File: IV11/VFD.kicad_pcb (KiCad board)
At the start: 2 copper layers, 225 x 80 mm, 71 parts, among them J1 USB_B, SW1 switch, SW2 switch, SW3 switch, SW4 switch, U1 74HC595, U10 UDN2981, U11 UDN2981, U12 UDN2981, U13 WeMos_mini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

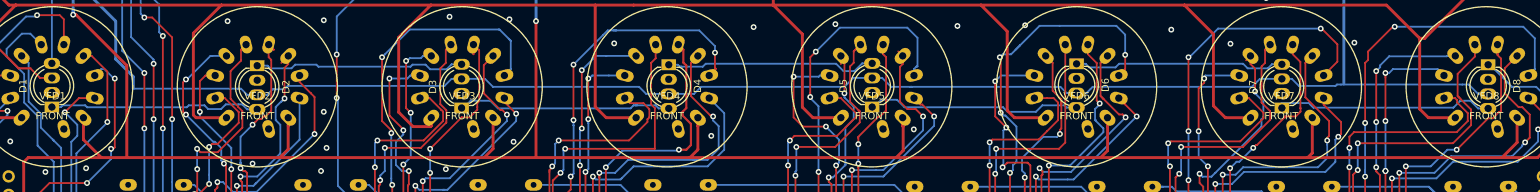
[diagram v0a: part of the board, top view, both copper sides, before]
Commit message: Make LED footprint pads slightly narrower (1.3mm) for easier solderingx
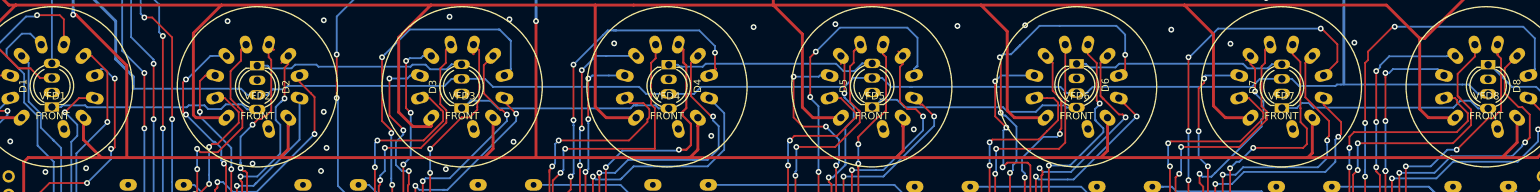
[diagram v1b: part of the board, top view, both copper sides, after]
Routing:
- net Net-(U16-Pad11): track 48.4 -> 52.2 mm
- net Net-(U16-Pad17): track 37.3 -> 36.6 mm

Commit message: s/chinesemodules/genericmodules
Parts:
- U18: footprint ChineseModules:BuckModule -> GenericModules:MP2307BuckConverterModule
- U19: footprint ChineseModules:MT3608BoostModule -> GenericModules:MT3608BoostConverterModule
- U20: footprint ChineseModules:DS3121RTCModule -> GenericModules:DS3121RTCModule
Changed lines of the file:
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@@
-(kicad_pcb (version 20171130) (host pcbnew 5.0.0-fee4fd1~66~ubuntu18.04.1)
+(kicad_pcb (version 20171130) (host pcbnew 5.0.0-fee4fd1~65~ubuntu17.10.1)
   (general
     (thickness 1.6)
@@
     )
   )
-  (module ChineseModules:BuckModule (layer B.Cu)
-    (at 113.538 19.812 180)
-    (fp_text reference U18 (at 0 2.286 180) (layer B.SilkS)
-      (effects (font (size 1 1) (thickness 0.15)) (justify mirror))
-    )
-    (fp_text value MiniBuckBoard (at 0 0.5 180) (layer B.Fab)
-      (effects (font (size 1 1) (thickness 0.15)) (justify mirror))
-    )
-    (fp_text user GND (at 5 -5 180) (layer B.SilkS)
-      (effects (font (size 1 1) (thickness 0.15)) (justify mirror))
-    )
-    (fp_text user GND (at -5 -5 180) (layer B.SilkS)
-      (effects (font (size 1 1) (thickness 0.15)) (justify mirror))
-    )
-    (fp_text user Vout (at -5 5 180) (layer B.SilkS)
-      (effects (font (size 1 1) (thickness 0.15)) (justify mirror))
-    )
-    (fp_text user Vin (at 5 5 180) (layer B.SilkS)
-      (effects (font (size 1 1) (thickness 0.15)) (justify mirror))
-    )
-    (fp_line (start -9.25 6) (end -9.25 -6) (layer B.SilkS) (width 0.15))
-    (fp_line (start -9.25 -6) (end 9.25 -6) (layer B.SilkS) (width 0.15))
-    (fp_line (start 9.25 6) (end 9.25 -6) (layer B.SilkS) (width 0.15))
-    (fp_line (start -9.25 6) (end 9.25 6) (layer B.SilkS) (width 0.15))
-    (pad 4 thru_hole oval (at 8 5 180) (size 2.4 1.6) (drill 1) (layers *.Cu *.Mask)
-      (net 147 +5V))
-    (pad 3 thru_hole oval (at 8 -5 180) (size 2.4 1.6) (drill 1) (layers *.Cu *.Mask)
-      (net 1 GND))
-    (pad 2 thru_hole oval (at -8 -5 180) (size 2.4 1.6) (drill 1) (layers *.Cu *.Mask)
-      (net 1 GND))
-    (pad 1 thru_hole oval (at -8 5 180) (size 2.4 1.6) (drill 1) (layers *.Cu *.Mask)
-      (net 12 +1V5))
-  )
   (module "" (layer F.Cu)
     (at 102.997 2.54)
@@
     )
   )
-  (module ChineseModules:MT3608BoostModule (layer B.Cu)
+  (module GenericModules:MP2307BuckConverterModule (layer B.Cu)
+    (at 113.538 19.812 180)
+    (fp_text reference U18 (at 0 -1 180) (layer B.SilkS)
+      (effects (font (size 1 1) (thickness 0.15)) (justify mirror))
+    )
+    (fp_text value MiniBuckBoard (at 0 0.5 180) (layer B.Fab)
+      (effects (font (size 1 1) (thickness 0.15)) (justify mirror))
+    )
+    (fp_line (start -9.25 6) (end 9.25 6) (layer B.SilkS) (width 0.15))
+    (fp_line (start 9.25 6) (end 9.25 -6) (layer B.SilkS) (width 0.15))
+    (fp_line (start -9.25 -6) (end 9.25 -6) (layer B.SilkS) (width 0.15))
+    (fp_line (start -9.25 6) (end -9.25 -6) (layer B.SilkS) (width 0.15))
+    (fp_text user Vin (at 5 5 180) (layer B.SilkS)
+      (effects (font (size 1 1) (thickness 0.15)) (justify mirror))
+    )
+    (fp_text user Vout (at -5 5 180) (layer B.SilkS)
+      (effects (font (size 1 1) (thickness 0.15)) (justify mirror))
+    )
+    (fp_text user GND (at -5 -5 180) (layer B.SilkS)
+      (effects (font (size 1 1) (thickness 0.15)) (justify mirror))
+    )
+    (fp_text user GND (at 5 -5 180) (layer B.SilkS)
+      (effects (font (size 1 1) (thickness 0.15)) (justify mirror))
+    )
+    (pad 1 thru_hole oval (at -8 5 180) (size 2.4 1.6) (drill 1) (layers *.Cu *.Mask)
+      (net 12 +1V5))
+    (pad 2 thru_hole oval (at -8 -5 180) (size 2.4 1.6) (drill 1) (layers *.Cu *.Mask)
+      (net 1 GND))
+    (pad 3 thru_hole oval (at 8 -5 180) (size 2.4 1.6) (drill 1) (layers *.Cu *.Mask)
+      (net 1 GND))
+    (pad 4 thru_hole oval (at 8 5 180) (size 2.4 1.6) (drill 1) (layers *.Cu *.Mask)
+      (net 147 +5V))
+  )
+  (module GenericModules:MT3608BoostConverterModule (layer B.Cu)
     (at 94.361 2.159 180)
     (fp_text reference U19 (at 15 -9 180) (layer B.SilkS)
@@
       (net 147 +5V))
   )
-  (module ChineseModules:DS3121RTCModule (layer B.Cu)
+  (module GenericModules:DS3121RTCModule (layer B.Cu)
     (at 143.002 9.779 180)
     (fp_text reference U20 (at 0 -2 180) (layer B.SilkS)
@@
       (effects (font (size 1 1) (thickness 0.15)) (justify mirror))
     )
-    (fp_text user UPPERMOST (at 0 -8 180) (layer B.SilkS)
+    (fp_line (start -19 9) (end 18.25 9) (layer B.SilkS) (width 0.15))
+    (fp_line (start -19 9) (end -19 -13.25) (layer B.SilkS) (width 0.15))
+    (fp_line (start -19 -13.25) (end 18.25 -13.25) (layer B.SilkS) (width 0.15))
+    (fp_line (start 18.25 9) (end 18.25 -13.25) (layer B.SilkS) (width 0.15))
+    (fp_text user "COIN CELL" (at 0 -6 180) (layer B.SilkS)
       (effects (font (size 1 1) (thickness 0.15)) (justify mirror))
     )
-    (fp_text user "COIN CELL" (at 0 -6 180) (layer B.SilkS)
+    (fp_text user UPPERMOST (at 0 -8 180) (layer B.SilkS)
       (effects (font (size 1 1) (thickness 0.15)) (justify mirror))
     )
-    (fp_line (start 18.25 9) (end 18.25 -13.25) (layer B.SilkS) (width 0.15))
-    (fp_line (start -19 -13.25) (end 18.25 -13.25) (layer B.SilkS) (width 0.15))
-    (fp_line (start -19 9) (end -19 -13.25) (layer B.SilkS) (width 0.15))
-    (fp_line (start -19 9) (end 18.25 9) (layer B.SilkS) (width 0.15))
-    (pad 6 thru_hole oval (at -17.25 -8.475 180) (size 2.4 1.6) (drill 1) (layers *.Cu *.Mask)
-      (net 152 "Net-(U20-Pad6)"))
-    (pad 7 thru_hole oval (at 16.5 -5.935 180) (size 2.4 1.6) (drill 1) (layers *.Cu *.Mask)
-      (net 155 "Net-(U20-Pad7)"))
-    (pad 8 thru_hole oval (at 16.5 -3.395 180) (size 2.4 1.6) (drill 1) (layers *.Cu *.Mask)
-      (net 154 "Net-(U20-Pad8)"))
-    (pad 9 thru_hole oval (at 16.5 -0.855 180) (size 2.4 1.6) (drill 1) (layers *.Cu *.Mask)
-      (net 153 "Net-(U20-Pad9)"))
-    (pad 10 thru_hole oval (at 16.5 1.685 180) (size 2.4 1.6) (drill 1) (layers *.Cu *.Mask)
-      (net 1 GND))
-    (pad 1 thru_hole oval (at -17.25 4.225 180) (size 2.4 1.6) (drill 1) (layers *.Cu *.Mask)
-      (net 1 GND))
-    (pad 2 thru_hole oval (at -17.25 1.685 180) (size 2.4 1.6) (drill 1) (layers *.Cu *.Mask)
-      (net 150 +3V3))
-    (pad 5 thru_hole oval (at -17.25 -5.935 180) (size 2.4 1.6) (drill 1) (layers *.Cu *.Mask)
-      (net 151 "Net-(U20-Pad5)"))
-    (pad 3 thru_hole oval (at -17.25 -0.855 180) (size 2.4 1.6) (drill 1) (layers *.Cu *.Mask)
-      (net 159 SDA))
     (pad 4 thru_hole oval (at -17.25 -3.395 180) (size 2.4 1.6) (drill 1) (layers *.Cu *.Mask)
       (net 158 SCL))
+    (pad 3 thru_hole oval (at -17.25 -0.855 180) (size 2.4 1.6) (drill 1) (layers *.Cu *.Mask)
+      (net 159 SDA))
+    (pad 5 thru_hole oval (at -17.25 -5.935 180) (size 2.4 1.6) (drill 1) (layers *.Cu *.Mask)
+      (net 151 "Net-(U20-Pad5)"))
+    (pad 2 thru_hole oval (at -17.25 1.685 180) (size 2.4 1.6) (drill 1) (layers *.Cu *.Mask)
+      (net 150 +3V3))
+    (pad 1 thru_hole oval (at -17.25 4.225 180) (size 2.4 1.6) (drill 1) (layers *.Cu *.Mask)
+      (net 1 GND))
+    (pad 10 thru_hole oval (at 16.5 1.685 180) (size 2.4 1.6) (drill 1) (layers *.Cu *.Mask)
+      (net 1 GND))
+    (pad 9 thru_hole oval (at 16.5 -0.855 180) (size 2.4 1.6) (drill 1) (layers *.Cu *.Mask)
+      (net 153 "Net-(U20-Pad9)"))
+    (pad 8 thru_hole oval (at 16.5 -3.395 180) (size 2.4 1.6) (drill 1) (layers *.Cu *.Mask)
+      (net 154 "Net-(U20-Pad8)"))
+    (pad 7 thru_hole oval (at 16.5 -5.935 180) (size 2.4 1.6) (drill 1) (layers *.Cu *.Mask)
+      (net 155 "Net-(U20-Pad7)"))
+    (pad 6 thru_hole oval (at -17.25 -8.475 180) (size 2.4 1.6) (drill 1) (layers *.Cu *.Mask)
+      (net 152 "Net-(U20-Pad6)"))
   )
   (gr_text "V1.1\n" (at 29.718 15.24) (layer B.SilkS)

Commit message: PCB updates - rerouted track for 3v3 to shift registers and refilled ground planes accordingly
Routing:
- net +3V3: track 747.6 -> 730.6 mm, vias 7 -> 2

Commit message: V1.1 board completed, + gerbers
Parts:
- added DS18B20: DS18B20, Connector_PinHeader_2.54mm:PinHeader_1x03_P2.54mm_Vertical, B.Cu at (213.9, 8.64)
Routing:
- net SW_1: track 215.2 -> 220.1 mm
- net +3V3: track 730.6 -> 733.5 mm
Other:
- board text added: "1"
- board text added: "2"
- board text added: "3"
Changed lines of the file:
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@@
   (general
     (thickness 1.6)
-    (drawings 7)
-    (tracks 2234)
+    (drawings 10)
+    (tracks 2241)
     (zones 0)
-    (modules 71)
+    (modules 72)
     (nets 174)
   )
@@
   )
   (setup
-    (last_trace_width 0.3)
+    (last_trace_width 0.25)
     (user_trace_width 0.3)
     (user_trace_width 0.4)
@@
       (net 152 "Net-(U20-Pad6)"))
   )
+  (module Connector_PinHeader_2.54mm:PinHeader_1x03_P2.54mm_Vertical (layer B.Cu)
+    (at 213.9188 8.636 180)
+    (descr "Through hole straight pin header, 1x03, 2.54mm pitch, single row")
+    (tags "Through hole pin header THT 1x03 2.54mm single row")
+    (fp_text reference DS18B20 (at -4.6228 -1.4732 180) (layer B.SilkS)
+      (effects (font (size 1 1) (thickness 0.15)) (justify mirror))
+    )
+    (fp_text value DS18B20 (at 0 -7.41 180) (layer B.Fab)
+      (effects (font (size 1 1) (thickness 0.15)) (justify mirror))
+    )
+    (fp_line (start -0.635 1.27) (end 1.27 1.27) (layer B.Fab) (width 0.1))
+    (fp_line (start 1.27 1.27) (end 1.27 -6.35) (layer B.Fab) (width 0.1))
+    (fp_line (start 1.27 -6.35) (end -1.27 -6.35) (layer B.Fab) (width 0.1))
+    (fp_line (start -1.27 -6.35) (end -1.27 0.635) (layer B.Fab) (width 0.1))
+    (fp_line (start -1.27 0.635) (end -0.635 1.27) (layer B.Fab) (width 0.1))
+    (fp_line (start -1.33 -6.41) (end 1.33 -6.41) (layer B.SilkS) (width 0.12))
+    (fp_line (start -1.33 -1.27) (end -1.33 -6.41) (layer B.SilkS) (width 0.12))
+    (fp_line (start 1.33 -1.27) (end 1.33 -6.41) (layer B.SilkS) (width 0.12))
+    (fp_line (start -1.33 -1.27) (end 1.33 -1.27) (layer B.SilkS) (width 0.12))
+    (fp_line (start -1.33 0) (end -1.33 1.33) (layer B.SilkS) (width 0.12))
+    (fp_line (start -1.33 1.33) (end 0 1.33) (layer B.SilkS) (width 0.12))
+    (fp_line (start -1.8 1.8) (end -1.8 -6.85) (layer B.CrtYd) (width 0.05))
+    (fp_line (start -1.8 -6.85) (end 1.8 -6.85) (layer B.CrtYd) (width 0.05))
+    (fp_line (start 1.8 -6.85) (end 1.8 1.8) (layer B.CrtYd) (width 0.05))
+    (fp_line (start 1.8 1.8) (end -1.8 1.8) (layer B.CrtYd) (width 0.05))
+    (fp_text user %R (at 0 -2.54 90) (layer B.Fab)
+      (effects (font (size 1 1) (thickness 0.15)) (justify mirror))
+    )
+    (pad 1 thru_hole rect (at 0 0 180) (size 1.7 1.7) (drill 1) (layers *.Cu *.Mask)
+      (net 1 GND))
+    (pad 2 thru_hole oval (at 0 -2.54 180) (size 1.7 1.7) (drill 1) (layers *.Cu *.Mask)
+      (net 26 SW_1))
+    (pad 3 thru_hole oval (at 0 -5.08 180) (size 1.7 1.7) (drill 1) (layers *.Cu *.Mask)
+      (net 150 +3V3))
+    (model ${KISYS3DMOD}/Connector_PinHeader_2.54mm.3dshapes/PinHeader_1x03_P2.54mm_Vertical.wrl
+      (at (xyz 0 0 0))
+      (scale (xyz 1 1 1))
+      (rotate (xyz 0 0 0))
+    )
+  )
+  (gr_text 1 (at 212 8.7376) (layer B.SilkS)
+    (effects (font (size 1 1) (thickness 0.25)) (justify mirror))
+  )
+  (gr_text 2 (at 212 11.0744) (layer B.SilkS)
+    (effects (font (size 1 1) (thickness 0.25)) (justify mirror))
+  )
+  (gr_text 3 (at 212 13.97) (layer B.SilkS)
+    (effects (font (size 1 1) (thickness 0.25)) (justify mirror))
+  )
   (gr_text "V1.1\n" (at 29.718 15.24) (layer B.SilkS)
     (effects (font (size 3 3) (thickness 0.3)) (justify mirror))
@@
   (segment (start 55.753 7.239) (end 90.805 7.239) (width 0.25) (layer B.Cu) (net 26))
   (segment (start 90.805 7.239) (end 91.44 7.239) (width 0.25) (layer B.Cu) (net 26))
-  (segment (start 209.150001 3.599999) (end 209.150001 12.718999) (width 0.25) (layer B.Cu) (net 26))
   (segment (start 210 2.75) (end 209.150001 3.599999) (width 0.25) (layer B.Cu) (net 26))
   (segment (start 203 18.869) (end 209.150001 12.718999) (width 0.25) (layer B.Cu) (net 26))
@@
   (segment (start 53.213 4.699) (end 55.353001 6.839001) (width 0.25) (layer F.Cu) (net 26))
   (segment (start 31.242 2.413) (end 33.528 4.699) (width 0.25) (layer F.Cu) (net 26))
+  (segment (start 213.9188 11.176) (end 209.251601 11.176) (width 0.25) (layer B.Cu) (net 26))
+  (segment (start 209.251601 11.176) (end 209.150001 11.2776) (width 0.25) (layer B.Cu) (net 26))
+  (segment (start 209.150001 3.599999) (end 209.150001 11.2776) (width 0.25) (layer B.Cu) (net 26))
+  (segment (start 209.150001 11.2776) (end 209.150001 12.718999) (width 0.25) (layer B.Cu) (net 26))
   (segment (start 28.702 3.685792) (end 30.985208 5.969) (width 0.25) (layer F.Cu) (net 27))
   (segment (start 28.702 2.413) (end 28.702 3.685792) (width 0.25) (layer F.Cu) (net 27))
@@
   (segment (start 199.009 66.941) (end 199.009 51.816) (width 0.25) (layer F.Cu) (net 145))
   (segment (start 199.009 51.816) (end 199.009 51.816) (width 0.25) (layer F.Cu) (net 145))
-  (via (at 199.009 51.816) (size 0.8) (drill 0.4) (layers F.Cu B.Cu) (net 145))
+  (via (at 199.009 51.816) (size 0.8) (drill 0.4) (layers F.Cu B.Cu) (net 145) (status 1000000))
   (segment (start 213.487 37.450501) (end 213.487 40.894) (width 0.25) (layer F.Cu) (net 145))
   (segment (start 215.180141 35.75736) (end 213.487 37.450501) (width 0.25) (layer F.Cu) (net 145))
@@
   (segment (start 218.726 18.92) (end 215.643 18.92) (width 0.4) (layer F.Cu) (net 150))
   (segment (start 206.723 10) (end 203 10) (width 0.4) (layer F.Cu) (net 150))
-  (segment (start 215.643 18.92) (end 206.723 10) (width 0.4) (layer F.Cu) (net 150))
   (segment (start 201.302944 10) (end 196 10) (width 0.4) (layer F.Cu) (net 150))
   (segment (start 203 10) (end 201.302944 10) (width 0.4) (layer F.Cu) (net 150))
@@
   (segment (start 46.101 0.762) (end 92.837 0.762) (width 0.4) (layer F.Cu) (net 150))
   (segment (start 213.995 71.5) (end 215.495 71.5) (width 0.3) (layer F.Cu) (net 150))
-  (segment (start 222.8088 23.0028) (end 218.726 18.92) (width 0.3) (layer F.Cu) (net 150))
-  (segment (start 222.8088 64.1862) (end 222.8088 23.0028) (width 0.3) (layer F.Cu) (net 150))
-  (segment (start 215.495 71.5) (end 222.8088 64.1862) (width 0.3) (layer F.Cu) (net 150))
+  (segment (start 222.8088 23.0028) (end 218.726 18.92) (width 0.4) (layer F.Cu) (net 150))
+  (segment (start 222.8088 64.1862) (end 222.8088 23.0028) (width 0.4) (layer F.Cu) (net 150))
+  (segment (start 215.495 71.5) (end 222.8088 64.1862) (width 0.4) (layer F.Cu) (net 150))
+  (segment (start 212.716719 13.716) (end 211.6582 14.774519) (width 0.25) (layer F.Cu) (net 150))
+  (segment (start 213.9188 13.716) (end 212.716719 13.716) (width 0.25) (layer F.Cu) (net 150))
+  (segment (start 211.6582 14.774519) (end 211.6582 14.9352) (width 0.25) (layer F.Cu) (net 150))
+  (segment (start 215.643 18.92) (end 211.6582 14.9352) (width 0.4) (layer F.Cu) (net 150))
+  (segment (start 211.6582 14.9352) (end 206.723 10) (width 0.4) (layer F.Cu) (net 150))
   (segment (start 35.814 5.715) (end 97.409 5.715) (width 0.25) (layer B.Cu) (net 156))
   (segment (start 34.671 4.572) (end 35.814 5.715) (width 0.25) (layer B.Cu) (net 156))

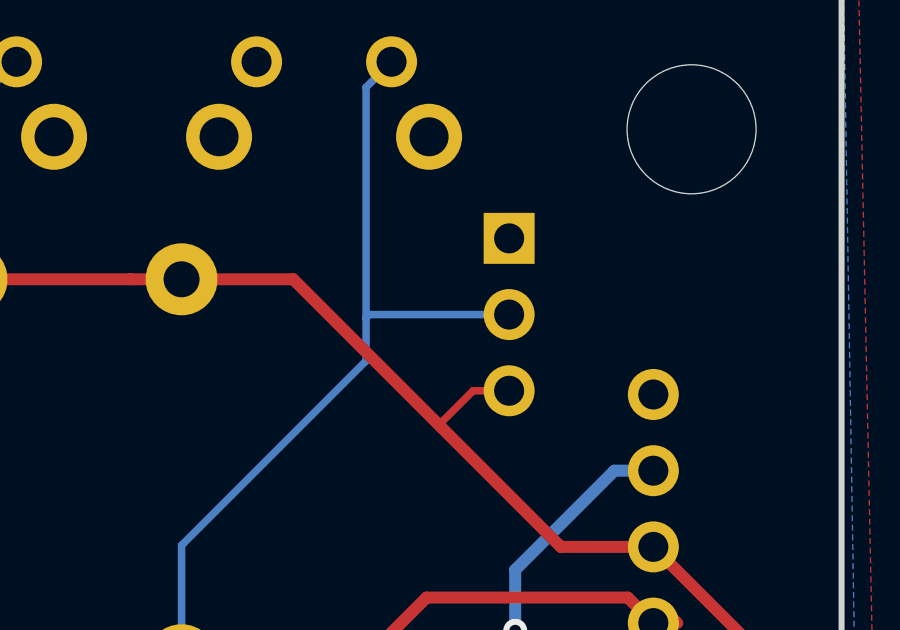
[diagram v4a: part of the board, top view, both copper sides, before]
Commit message: Fix problems with switches not being connected to ground
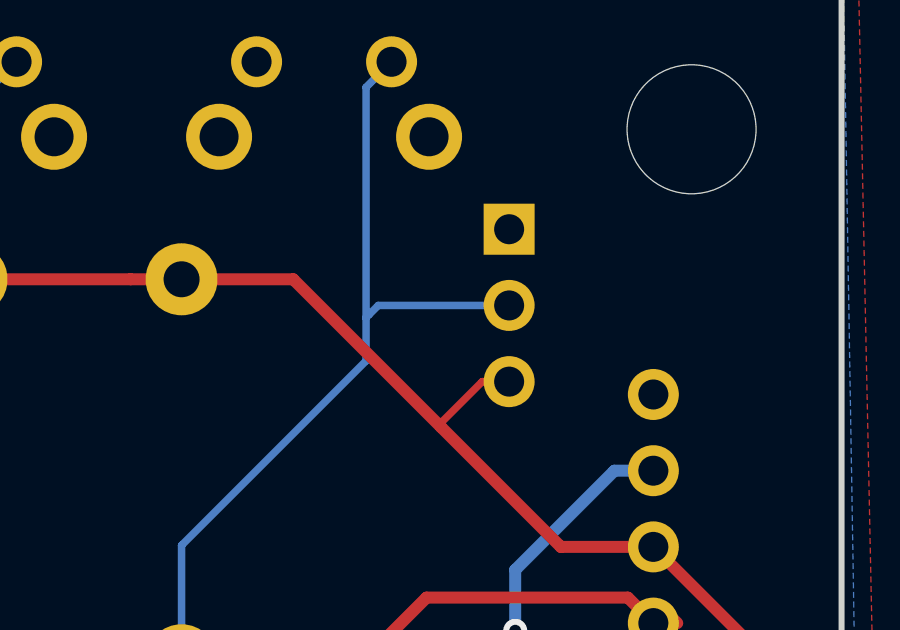
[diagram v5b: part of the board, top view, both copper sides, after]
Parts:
- moved DS18B20 0.30 mm to (213.9, 8.33)
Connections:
- SW2 pad 2: Net-(SW2-Pad2) -> GND
- SW3 pad 2: Net-(SW3-Pad2) -> GND
- SW4 pad 2: Net-(SW4-Pad2) -> GND

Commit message: Update version number (now 1.2). Sigh.
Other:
- board text added: "V1.2"
- board text removed: "V1.1"
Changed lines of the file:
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@@
     (effects (font (size 1 1) (thickness 0.25)) (justify mirror))
   )
-  (gr_text "V1.1\n" (at 29.718 15.24) (layer B.SilkS)
+  (gr_text V1.2 (at 29.718 15.24) (layer B.SilkS)
     (effects (font (size 3 3) (thickness 0.3)) (justify mirror))
   )
